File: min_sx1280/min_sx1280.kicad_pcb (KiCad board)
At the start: 2 copper layers, 20.5 x 17.4 mm, 15 parts, among them J1 Conn_01x04, SW1 SW_SPST, U1 ME6211C33, U2 ESP-01F, U3 LoRa1280

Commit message: Minimal RX ready to route
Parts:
- C1, C2, C5, C6: footprint Capacitor_Tantalum_SMD:CP_EIA-1608-08_AVX-J_Pad1.25x1.05mm_HandSolder -> Capacitor_Tantalum_SMD:CP_EIA-1608-08_AVX-J
- C3, C4: footprint Capacitor_SMD:C_0603_1608Metric_Pad1.05x0.95mm_HandSolder -> Capacitor_SMD:C_0603_1608Metric
- D1: footprint LED_SMD:LED_0603_1608Metric_Pad1.05x0.95mm_HandSolder -> LED_SMD:LED_0603_1608Metric
- R3, R4: footprint Resistor_SMD:R_0603_1608Metric_Pad1.05x0.95mm_HandSolder -> Resistor_SMD:R_0603_1608Metric
- SW1: footprint Button_Switch_SMD:SW_SPST_EVQPE1 -> ELRS_lib:SW_3x4x2
- moved C3 11.2 mm to (111.3, 140.2), turned to -90 degrees
- moved C6 10.0 mm to (101.2, 130.4)
- moved C5 7.60 mm to (113.1, 140.3)
- moved C4 6.65 mm to (101.2, 133.9)
- moved R3 5.16 mm to (101.2, 137.9), turned to -90 degrees
- moved C1 3.09 mm to (107.5, 141.1)
- moved C2 3.05 mm to (107.5, 139.5)
- moved U1 3.05 mm to (104.0, 140.5)
- moved U2 2.43 mm to (108.8, 133.2)
- moved SW1 0.44 mm to (117.6, 131.7)
- moved AE2 0.39 mm to (116.9, 141.8)
- moved D1 0.07 mm to (118.0, 136.4)
- moved R4 0.07 mm to (118.0, 137.9)
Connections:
- U2 pad 1: (no net) -> Net-(U2-Pad1)
- U2 pad 16: (no net) -> /RST
- U2 pad 3: (no net) -> Net-(U2-Pad3)
- U2 pad 4: (no net) -> /EN
- U3 pad 1: (no net) -> Net-(U3-Pad1)
- U3 pad 2: (no net) -> Net-(U3-Pad2)
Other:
- board size 20.5 x 17.4 mm -> 19.8 x 16.8 mm

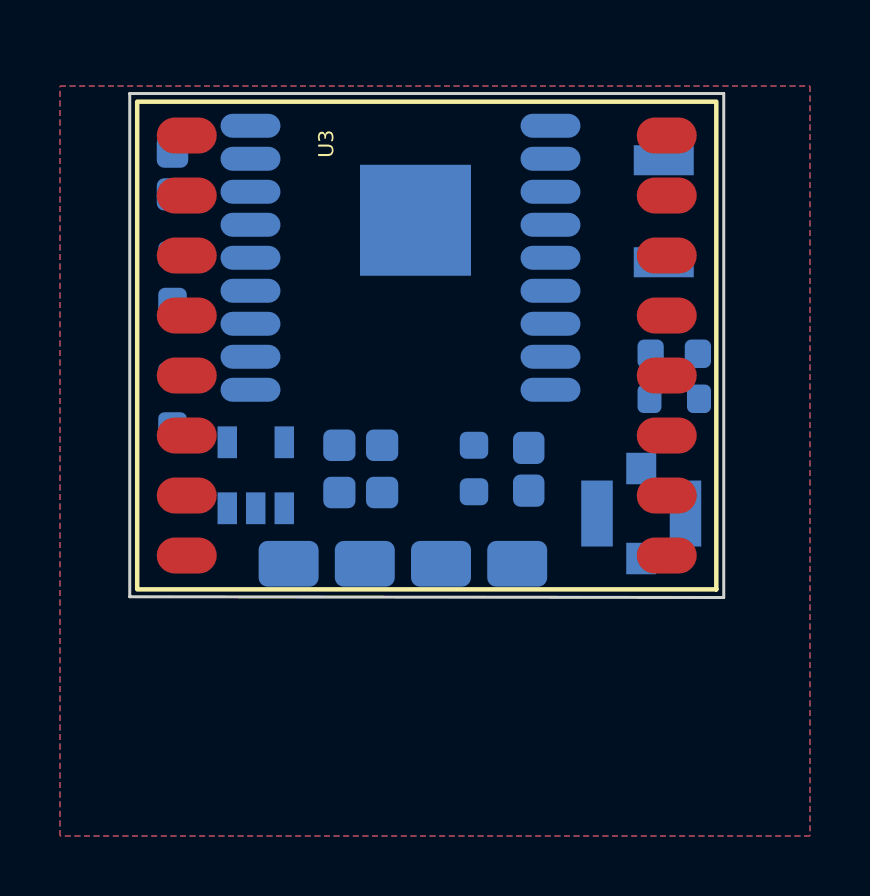
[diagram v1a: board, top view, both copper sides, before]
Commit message: Min RX routing done
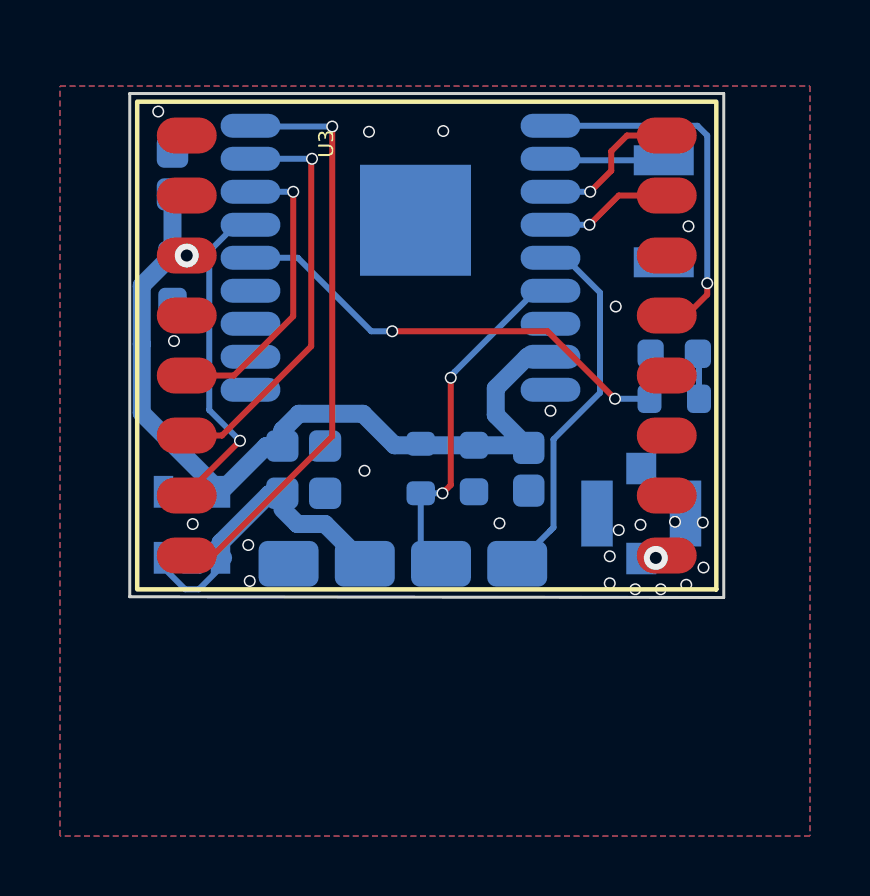
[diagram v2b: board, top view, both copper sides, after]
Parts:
- moved R3 8.59 mm to (109.5, 140.2)
- moved U1 2.69 mm to (101.9, 142.1)
- moved C2 1.90 mm to (105.6, 139.5)
- moved C1 1.90 mm to (105.6, 141.1)
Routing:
- net +3V3: track 0.00 -> 28.7 mm, vias 0 -> 1
- net /NSS: track 0.00 -> 19.6 mm, vias 0 -> 1
- net /IO16: track 0.00 -> 15.2 mm, vias 0 -> 2
- net /MOSI: track 0.00 -> 13.7 mm, vias 0 -> 1
- net /RX: track 0.00 -> 12.3 mm
- net /NRESET: track 0.00 -> 12.3 mm, vias 0 -> 1
- net /TX: track 0.00 -> 11.9 mm, vias 0 -> 2
- net /SCK: track 0.00 -> 11.0 mm, vias 0 -> 1
- net /MISO: track 0.00 -> 10.8 mm, vias 0 -> 1
- net +5V: track 0.00 -> 9.99 mm
- net /DIO1: track 0.00 -> 5.03 mm, vias 0 -> 1
- net /BUSY: track 0.00 -> 4.28 mm, vias 0 -> 1
- net /BOOT: track 0.00 -> 3.80 mm
- net Net-(D1-Pad2): track 0.00 -> 1.52 mm
- net Net-(AE2-Pad1): track 0.00 -> 0.89 mm, vias 0 -> 1
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
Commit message: Last tweaks and gerber files to min_sx1280 and e28_tx
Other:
- board text added: "JLCJLCJLCJLC"
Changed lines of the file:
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@@
   (setup
     (stackup
-      (layer "F.SilkS" (type "Top Silk Screen"))
+      (layer "F.SilkS" (type "Top Silk Screen") (color "White"))
       (layer "F.Paste" (type "Top Solder Paste"))
       (layer "F.Mask" (type "Top Solder Mask") (color "Green") (thickness 0.01))
@@
       (layer "B.Mask" (type "Bottom Solder Mask") (color "Green") (thickness 0.01))
       (layer "B.Paste" (type "Bottom Solder Paste"))
-      (layer "B.SilkS" (type "Bottom Silk Screen"))
+      (layer "B.SilkS" (type "Bottom Silk Screen") (color "White"))
       (copper_finish "None")
       (dielectric_constraints no)
     )
+    (aux_axis_origin 99.819 144.532)
     (pcbplotparams
-      (layerselection 0x00010fc_ffffffff)
+      (layerselection 0x00010f0_ffffffff)
       (disableapertmacros false)
-      (usegerberextensions false)
+      (usegerberextensions true)
       (usegerberattributes true)
       (usegerberadvancedattributes true)
@@
       (viasonmask false)
       (mode 1)
-      (useauxorigin false)
+      (useauxorigin true)
       (hpglpennumber 1)
       (hpglpenspeed 20)
@@
       (psa4output false)
       (plotreference true)
-      (plotvalue true)
+      (plotvalue false)
       (plotinvisibletext false)
       (sketchpadsonfab false)
@@
       (outputformat 1)
       (mirror false)
-      (drillshape 1)
+      (drillshape 0)
       (scaleselection 1)
-      (outputdirectory "")
+      (outputdirectory "Gerber")
     )
   )
@@
       (rotate (xyz 0 0 0))
     )
+    (model "C:/Users/Alberto/Documents/Kicad/ExpressLRS_HW_stuff/ELRS_lib/3d_lib/sx1280v1.step"
+      (offset (xyz -8 -8 0))
+      (scale (xyz 1 1 1))
+      (rotate (xyz 0 0 0))
+    )
   )
   (module "Capacitor_Tantalum_SMD:CP_EIA-1608-08_AVX-J" (layer "B.Cu")
@@
     (property "Sheet name" "")
     (attr smd)
-    (fp_text reference "C5" (at 1.375 -0.775 90) (layer "B.SilkS")
+    (fp_text reference "C5" (at 1.457 -0.921 90) (layer "B.SilkS")
       (effects (font (size 0.5 0.5) (thickness 0.15)) (justify mirror))
     )
@@
     (fp_line (start -0.8 0.125) (end -0.8 -0.425) (layer "B.Fab") (width 0.1))
     (fp_line (start -0.8 -0.425) (end 0.8 -0.425) (layer "B.Fab") (width 0.1))
-    (pad "1" smd roundrect (at -0.7125 0 270) (size 1.075 1.05) (layers "B.Cu" "B.Paste" "B.Mask") (roundrect_rratio 0.238095)
+    (pad "1" smd roundrect (at -0.7125 0 270) (size 1.075 1.05) (layers "B.Cu" "B.Paste" "B.Mask") (roundrect_rratio 0.2380952380952381)
       (net 4 "+3V3"))
-    (pad "2" smd roundrect (at 0.7125 0 270) (size 1.075 1.05) (layers "B.Cu" "B.Paste" "B.Mask") (roundrect_rratio 0.238095)
+    (pad "2" smd roundrect (at 0.7125 0 270) (size 1.075 1.05) (layers "B.Cu" "B.Paste" "B.Mask") (roundrect_rratio 0.2380952380952381)
       (net 1 "GND"))
     (model "${KISYS3DMOD}/Capacitor_Tantalum_SMD.3dshapes/CP_EIA-1608-08_AVX-J.wrl"
@@
     (fp_line (start -0.8 0.125) (end -0.8 -0.425) (layer "B.Fab") (width 0.1))
     (fp_line (start 0.8 0.425) (end -0.5 0.425) (layer "B.Fab") (width 0.1))
-    (pad "1" smd roundrect (at -0.7125 0 90) (size 1.075 1.05) (layers "B.Cu" "B.Paste" "B.Mask") (roundrect_rratio 0.238095)
+    (pad "1" smd roundrect (at -0.7125 0 90) (size 1.075 1.05) (layers "B.Cu" "B.Paste" "B.Mask") (roundrect_rratio 0.2380952380952381)
       (net 4 "+3V3"))
-    (pad "2" smd roundrect (at 0.7125 0 90) (size 1.075 1.05) (layers "B.Cu" "B.Paste" "B.Mask") (roundrect_rratio 0.238095)
+    (pad "2" smd roundrect (at 0.7125 0 90) (size 1.075 1.05) (layers "B.Cu" "B.Paste" "B.Mask") (roundrect_rratio 0.2380952380952381)
       (net 1 "GND"))
     (model "${KISYS3DMOD}/Capacitor_Tantalum_SMD.3dshapes/CP_EIA-1608-08_AVX-J.wrl"
@@
       (net 1 "GND") (pinfunction "B"))
     (model "/home/remy/Documents/GitHub/ExpressLRS_HW_stuff/ELRS_lib/3d_lib/b3u-1000p.stp"
+      (offset (xyz 0 0 0))
+      (scale (xyz 1 1 1))
+      (rotate (xyz -90 0 0))
+    )
+    (model "C:/Users/Alberto/Documents/Kicad/ExpressLRS_HW_stuff/ELRS_lib/3d_lib/b3u-1000p.stp"
       (offset (xyz 0 0 0))
       (scale (xyz 1 1 1))
@@
     (fp_line (start 0.8 -0.425) (end 0.8 0.425) (layer "B.Fab") (width 0.1))
     (fp_line (start 0.8 0.425) (end -0.5 0.425) (layer "B.Fab") (width 0.1))
-    (pad "1" smd roundrect (at -0.7125 0) (size 1.075 1.05) (layers "B.Cu" "B.Paste" "B.Mask") (roundrect_rratio 0.238095)
+    (pad "1" smd roundrect (at -0.7125 0) (size 1.075 1.05) (layers "B.Cu" "B.Paste" "B.Mask") (roundrect_rratio 0.2380952380952381)
       (net 3 "+5V"))
-    (pad "2" smd roundrect (at 0.7125 0) (size 1.075 1.05) (layers "B.Cu" "B.Paste" "B.Mask") (roundrect_rratio 0.238095)
+    (pad "2" smd roundrect (at 0.7125 0) (size 1.075 1.05) (layers "B.Cu" "B.Paste" "B.Mask") (roundrect_rratio 0.2380952380952381)
       (net 1 "GND"))
     (model "${KISYS3DMOD}/Capacitor_Tantalum_SMD.3dshapes/CP_EIA-1608-08_AVX-J.wrl"
@@
     (fp_line (start -0.8 -0.425) (end 0.8 -0.425) (layer "B.Fab") (width 0.1))
     (fp_line (start -0.5 0.425) (end -0.8 0.125) (layer "B.Fab") (width 0.1))
-    (pad "1" smd roundrect (at -0.7125 0) (size 1.075 1.05) (layers "B.Cu" "B.Paste" "B.Mask") (roundrect_rratio 0.238095)
+    (pad "1" smd roundrect (at -0.7125 0) (size 1.075 1.05) (layers "B.Cu" "B.Paste" "B.Mask") (roundrect_rratio 0.2380952380952381)
       (net 4 "+3V3"))
-    (pad "2" smd roundrect (at 0.7125 0) (size 1.075 1.05) (layers "B.Cu" "B.Paste" "B.Mask") (roundrect_rratio 0.238095)
+    (pad "2" smd roundrect (at 0.7125 0) (size 1.075 1.05) (layers "B.Cu" "B.Paste" "B.Mask") (roundrect_rratio 0.2380952380952381)
       (net 1 "GND"))
     (model "${KISYS3DMOD}/Capacitor_Tantalum_SMD.3dshapes/CP_EIA-1608-08_AVX-J.wrl"
@@
       (rotate (xyz 0 0 0))
     )
+    (model "C:/Users/Alberto/Documents/Kicad/ExpressLRS_HW_stuff/ELRS_lib/3d_lib/esp01f v1.step"
+      (offset (xyz -5 -5.5 0))
+      (scale (xyz 1 1 1))
+      (rotate (xyz 0 0 0))
+    )
   )
   (module "ELRS_lib:U.FL" (layer "B.Cu")
@@
       (rotate (xyz -90 180 -90))
     )
+    (model "C:/Users/Alberto/Documents/Kicad/ExpressLRS_HW_stuff/ELRS_lib/3d_lib/u_fl-r-smt-1_10_.stp"
+      (offset (xyz -1.1 55.25 22.5))
+      (scale (xyz 1 1 1))
+      (rotate (xyz 90 0 90))
+    )
   )
   (gr_line (start 119.625 127.75) (end 99.825 127.75) (layer "Edge.Cuts") (width 0.1))
@@
     (effects (font (size 0.5 0.5) (thickness 0.125)) (justify mirror))
   )
+  (gr_text "JLCJLCJLCJLC" (at 112.54 136.13 90) (layer "F.SilkS")
+    (effects (font (size 1.5 1.5) (thickness 0.3)))
+  )
   (dimension (type aligned) (layer "Dwgs.User")
     (pts (xy 120 144.9) (xy 120 127.5))
@@
   (via (at 118 142.025) (size 0.4) (drill 0.3) (layers "F.Cu" "B.Cu") (net 1))
   (via (at 115.825 143.175) (size 0.4) (drill 0.3) (layers "F.Cu" "B.Cu") (net 1))
-  (via (at 101.925 142.1) (size 0.4) (drill 0.3) (layers "F.Cu" "B.Cu") (net 1))
+  (via (at 100.711 142.125) (size 0.4) (drill 0.3) (layers "F.Cu" "B.Cu") (net 1))
   (via (at 118.45 132.175) (size 0.4) (drill 0.3) (layers "F.Cu" "B.Cu") (net 1))
   (via (at 107.65 140.325) (size 0.4) (drill 0.3) (layers "F.Cu" "B.Cu") (net 1))
   (via (at 116.675 144.275) (size 0.4) (drill 0.3) (layers "F.Cu" "B.Cu") (net 1))
-  (via (at 100.775 128.35) (size 0.4) (drill 0.3) (layers "F.Cu" "B.Cu") (net 1))
+  (via (at 100.584 128.35) (size 0.4) (drill 0.3) (layers "F.Cu" "B.Cu") (net 1))
   (via (at 113.85 138.325) (size 0.4) (drill 0.3) (layers "F.Cu" "B.Cu") (net 1))
   (via (at 116.125 142.3) (size 0.4) (drill 0.3) (layers "F.Cu" "B.Cu") (net 1))
   (via (at 118.925 142.05) (size 0.4) (drill 0.3) (layers "F.Cu" "B.Cu") (net 1))
   (via (at 101.3 136) (size 0.4) (drill 0.3) (layers "F.Cu" "B.Cu") (net 1))
-  (via (at 118.95 143.55) (size 0.4) (drill 0.3) (layers "F.Cu" "B.Cu") (net 1))
+  (via (at 119.126 143.55) (size 0.4) (drill 0.3) (layers "F.Cu" "B.Cu") (net 1))
   (via (at 117.525 144.275) (size 0.4) (drill 0.3) (layers "F.Cu" "B.Cu") (net 1))
   (via (at 116.025 134.85) (size 0.4) (drill 0.3) (layers "F.Cu" "B.Cu") (net 1))
@@
   (via (at 110.275 129) (size 0.4) (drill 0.3) (layers "F.Cu" "B.Cu") (net 1))
   (via (at 103.825 144) (size 0.4) (drill 0.3) (layers "F.Cu" "B.Cu") (net 1))
-  (via (at 118.375 144.125) (size 0.4) (drill 0.3) (layers "F.Cu" "B.Cu") (net 1))
+  (via (at 118.618 144.145) (size 0.4) (drill 0.3) (layers "F.Cu" "B.Cu") (net 1))
   (segment (start 117.725 143.15) (end 117.440568 143.15) (width 0.4) (layer "F.Cu") (net 2))
   (segment (start 117.440568 143.15) (end 117.360625 143.229943) (width 0.4) (layer "F.Cu") (net 2))
@@
     (polygon
       (pts
-        (xy 122.5 152.5)
-        (xy 97.5 152.5)
-        (xy 97.5 127.5)
-        (xy 122.5 127.5)
+        (xy 120.131557 144.754413)
+        (xy 99.568 144.78)
+        (xy 99.568 127.635)
+        (xy 120.142 127.762)
       )
     )
@@
     (polygon
       (pts
-        (xy 122.5 152.5)
-        (xy 97.5 152.5)
-        (xy 97.5 127.5)
-        (xy 122.5 127.5)
+        (xy 120.131557 144.754413)
+        (xy 99.568 144.78)
+        (xy 99.568 127.635)
+        (xy 120.142 127.762)
       )
     )
